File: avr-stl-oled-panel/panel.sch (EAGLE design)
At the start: 13 parts

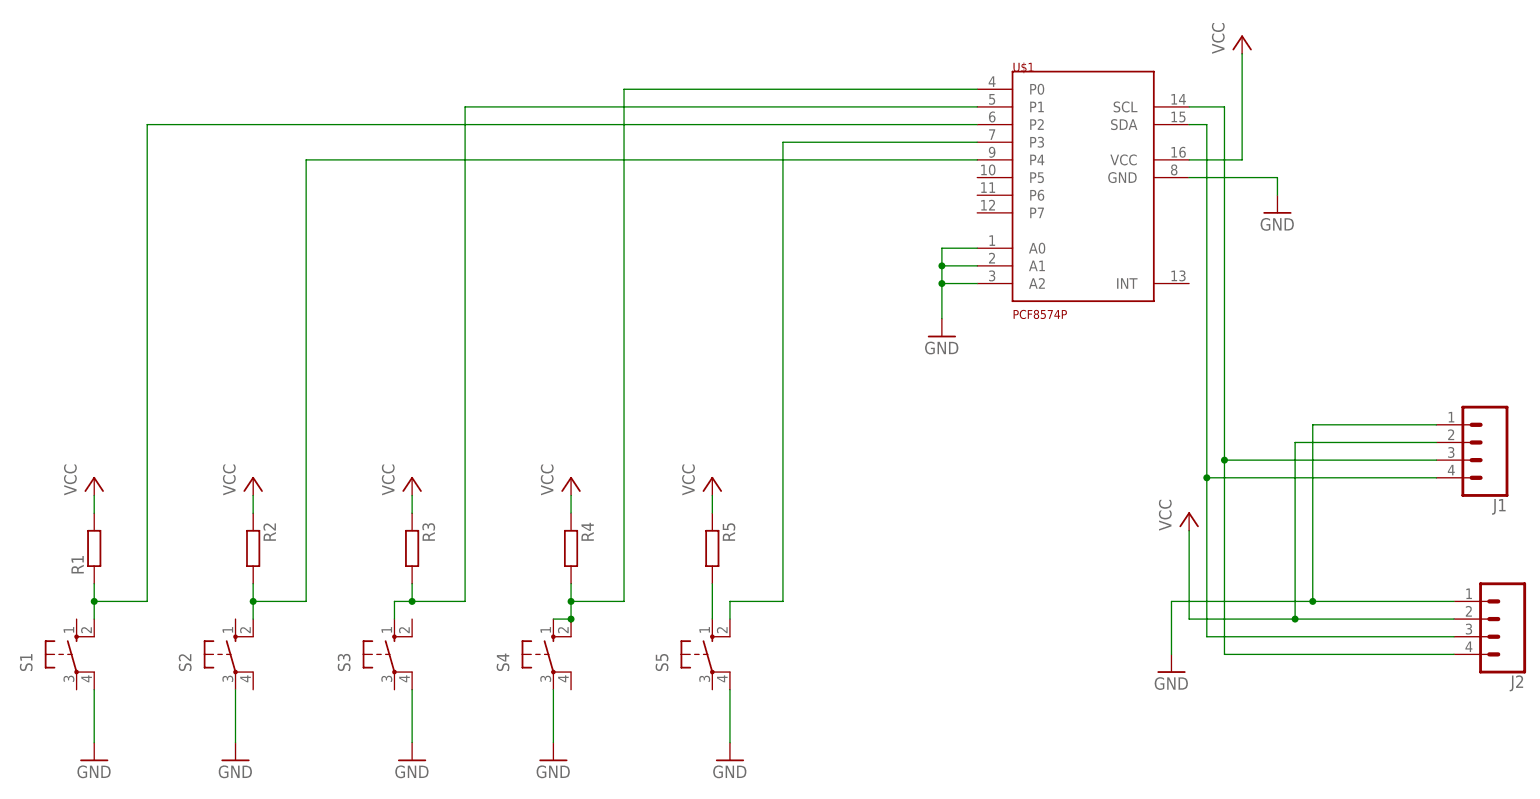
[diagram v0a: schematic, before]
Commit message: changing oled panel chip to smd
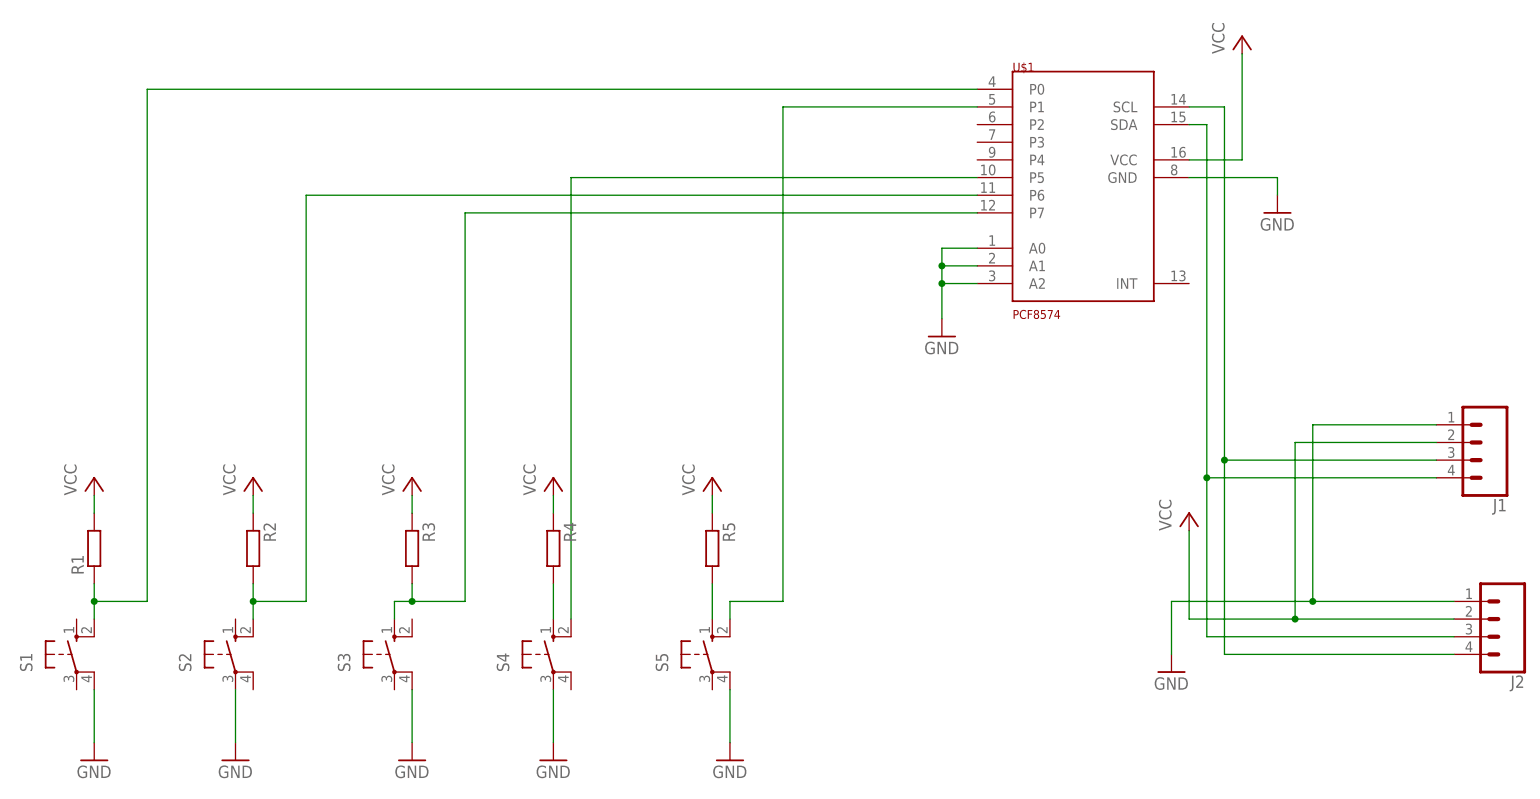
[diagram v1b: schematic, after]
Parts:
- U$1: value PCF8574P -> PCF8574; device pcf8574p:PCF8574P -> pcf8574p:PCF8574
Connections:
- new net N$2: R4.2, S4.S
- net B0: now also U$1.P0; no longer U$1.P2
- net B1: now also U$1.P6; no longer U$1.P4
- net B2: now also U$1.P7; no longer U$1.P1
- net B3: now also U$1.P5; no longer R4.2, S4.S, U$1.P0
- net B4: now also U$1.P1; no longer U$1.P3
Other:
- moved on the sheet: R4
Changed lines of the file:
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@@
 <part name="P+5" library="supply1" deviceset="VCC" device=""/>
 <part name="GND6" library="supply1" deviceset="GND" device=""/>
-<part name="U$1" library="pcf8574p" deviceset="PCF8574P" device=""/>
+<part name="U$1" library="pcf8574p" deviceset="PCF8574" device=""/>
 <part name="GND7" library="supply1" deviceset="GND" device=""/>
 <part name="P+6" library="supply1" deviceset="VCC" device=""/>
@@
 <instance part="R2" gate="G$1" x="-40.64" y="20.32" rot="R270"/>
 <instance part="R3" gate="G$1" x="-17.78" y="20.32" rot="R270"/>
-<instance part="R4" gate="G$1" x="5.08" y="20.32" rot="R270"/>
+<instance part="R4" gate="G$1" x="2.54" y="20.32" rot="R270"/>
 <instance part="R5" gate="G$1" x="25.4" y="20.32" rot="R270"/>
 <instance part="P+1" gate="VCC" x="-63.5" y="30.48"/>
@@
 <instance part="P+2" gate="VCC" x="-40.64" y="30.48"/>
 <instance part="P+3" gate="VCC" x="-17.78" y="30.48"/>
-<instance part="P+4" gate="VCC" x="5.08" y="30.48"/>
+<instance part="P+4" gate="VCC" x="2.54" y="30.48"/>
 <instance part="P+5" gate="VCC" x="25.4" y="30.48"/>
 <instance part="GND6" gate="1" x="58.42" y="50.8"/>
@@
 <net name="B0" class="0">
 <segment>
+<pinref part="U$1" gate="G$1" pin="P0"/>
+<wire x1="63.5" y1="86.36" x2="-55.88" y2="86.36" width="0.1524" layer="91"/>
+<pinref part="S1" gate="1" pin="S1"/>
 <pinref part="R1" gate="G$1" pin="1"/>
-<pinref part="S1" gate="1" pin="S1"/>
 <wire x1="-63.5" y1="15.24" x2="-63.5" y2="12.7" width="0.1524" layer="91"/>
 <wire x1="-63.5" y1="12.7" x2="-63.5" y2="10.16" width="0.1524" layer="91"/>
+<junction x="-63.5" y="12.7"/>
 <wire x1="-63.5" y1="12.7" x2="-55.88" y2="12.7" width="0.1524" layer="91"/>
-<wire x1="-55.88" y1="12.7" x2="-55.88" y2="81.28" width="0.1524" layer="91"/>
-<junction x="-63.5" y="12.7"/>
-<pinref part="U$1" gate="G$1" pin="P2"/>
-<wire x1="63.5" y1="81.28" x2="-55.88" y2="81.28" width="0.1524" layer="91"/>
+<wire x1="-55.88" y1="12.7" x2="-55.88" y2="86.36" width="0.1524" layer="91"/>
 </segment>
 </net>
@@
 <pinref part="P+4" gate="VCC" pin="VCC"/>
 <pinref part="R4" gate="G$1" pin="1"/>
-<wire x1="5.08" y1="27.94" x2="5.08" y2="25.4" width="0.1524" layer="91"/>
+<wire x1="2.54" y1="27.94" x2="2.54" y2="25.4" width="0.1524" layer="91"/>
 </segment>
 <segment>
@@
 <wire x1="-40.64" y1="12.7" x2="-40.64" y2="10.16" width="0.1524" layer="91"/>
 <wire x1="-40.64" y1="12.7" x2="-33.02" y2="12.7" width="0.1524" layer="91"/>
-<wire x1="-33.02" y1="12.7" x2="-33.02" y2="76.2" width="0.1524" layer="91"/>
+<wire x1="-33.02" y1="12.7" x2="-33.02" y2="71.12" width="0.1524" layer="91"/>
 <junction x="-40.64" y="12.7"/>
-<pinref part="U$1" gate="G$1" pin="P4"/>
-<wire x1="63.5" y1="76.2" x2="-33.02" y2="76.2" width="0.1524" layer="91"/>
+<pinref part="U$1" gate="G$1" pin="P6"/>
+<wire x1="63.5" y1="71.12" x2="-33.02" y2="71.12" width="0.1524" layer="91"/>
 </segment>
 </net>
@@
 <wire x1="-17.78" y1="15.24" x2="-17.78" y2="12.7" width="0.1524" layer="91"/>
 <wire x1="-17.78" y1="12.7" x2="-10.16" y2="12.7" width="0.1524" layer="91"/>
-<wire x1="-10.16" y1="12.7" x2="-10.16" y2="83.82" width="0.1524" layer="91"/>
+<wire x1="-10.16" y1="12.7" x2="-10.16" y2="68.58" width="0.1524" layer="91"/>
 <junction x="-17.78" y="12.7"/>
 <pinref part="S3" gate="1" pin="S"/>
-<pinref part="U$1" gate="G$1" pin="P1"/>
-<wire x1="63.5" y1="83.82" x2="-10.16" y2="83.82" width="0.1524" layer="91"/>
 <wire x1="-17.78" y1="12.7" x2="-20.32" y2="12.7" width="0.1524" layer="91"/>
 <wire x1="-20.32" y1="12.7" x2="-20.32" y2="10.16" width="0.1524" layer="91"/>
+<pinref part="U$1" gate="G$1" pin="P7"/>
+<wire x1="63.5" y1="68.58" x2="-10.16" y2="68.58" width="0.1524" layer="91"/>
 </segment>
 </net>
 <net name="B3" class="0">
 <segment>
-<pinref part="R4" gate="G$1" pin="2"/>
+<pinref part="U$1" gate="G$1" pin="P5"/>
+<wire x1="63.5" y1="73.66" x2="5.08" y2="73.66" width="0.1524" layer="91"/>
+<wire x1="5.08" y1="10.16" x2="5.08" y2="73.66" width="0.1524" layer="91"/>
 <pinref part="S4" gate="1" pin="S1"/>
-<wire x1="5.08" y1="15.24" x2="5.08" y2="12.7" width="0.1524" layer="91"/>
-<wire x1="5.08" y1="12.7" x2="5.08" y2="10.16" width="0.1524" layer="91"/>
-<wire x1="5.08" y1="12.7" x2="12.7" y2="12.7" width="0.1524" layer="91"/>
-<wire x1="12.7" y1="12.7" x2="12.7" y2="86.36" width="0.1524" layer="91"/>
-<junction x="5.08" y="12.7"/>
-<pinref part="S4" gate="1" pin="S"/>
-<wire x1="2.54" y1="10.16" x2="5.08" y2="10.16" width="0.1524" layer="91"/>
-<junction x="5.08" y="10.16"/>
-<pinref part="U$1" gate="G$1" pin="P0"/>
-<wire x1="12.7" y1="86.36" x2="63.5" y2="86.36" width="0.1524" layer="91"/>
 </segment>
 </net>
@@
 <wire x1="27.94" y1="12.7" x2="27.94" y2="10.16" width="0.1524" layer="91"/>
 <wire x1="27.94" y1="12.7" x2="35.56" y2="12.7" width="0.1524" layer="91"/>
-<wire x1="35.56" y1="12.7" x2="35.56" y2="78.74" width="0.1524" layer="91"/>
-<pinref part="U$1" gate="G$1" pin="P3"/>
-<wire x1="63.5" y1="78.74" x2="35.56" y2="78.74" width="0.1524" layer="91"/>
+<wire x1="35.56" y1="12.7" x2="35.56" y2="83.82" width="0.1524" layer="91"/>
+<pinref part="U$1" gate="G$1" pin="P1"/>
+<wire x1="63.5" y1="83.82" x2="35.56" y2="83.82" width="0.1524" layer="91"/>
 </segment>
 </net>
@@
 </segment>
 </net>
+<net name="N$2" class="0">
+<segment>
+<pinref part="R4" gate="G$1" pin="2"/>
+<pinref part="S4" gate="1" pin="S"/>
+<wire x1="2.54" y1="15.24" x2="2.54" y2="10.16" width="0.1524" layer="91"/>
+</segment>
+</net>
